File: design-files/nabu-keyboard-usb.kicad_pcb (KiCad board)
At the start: 2 copper layers, 55.2 x 71.8 mm, 20 parts, among them J1 Console UART header, J2 DIN-6, J3 9V input, Q1 IRLU110PBF, U1 74LVC245, U2 Pico, U3 SN75176AP

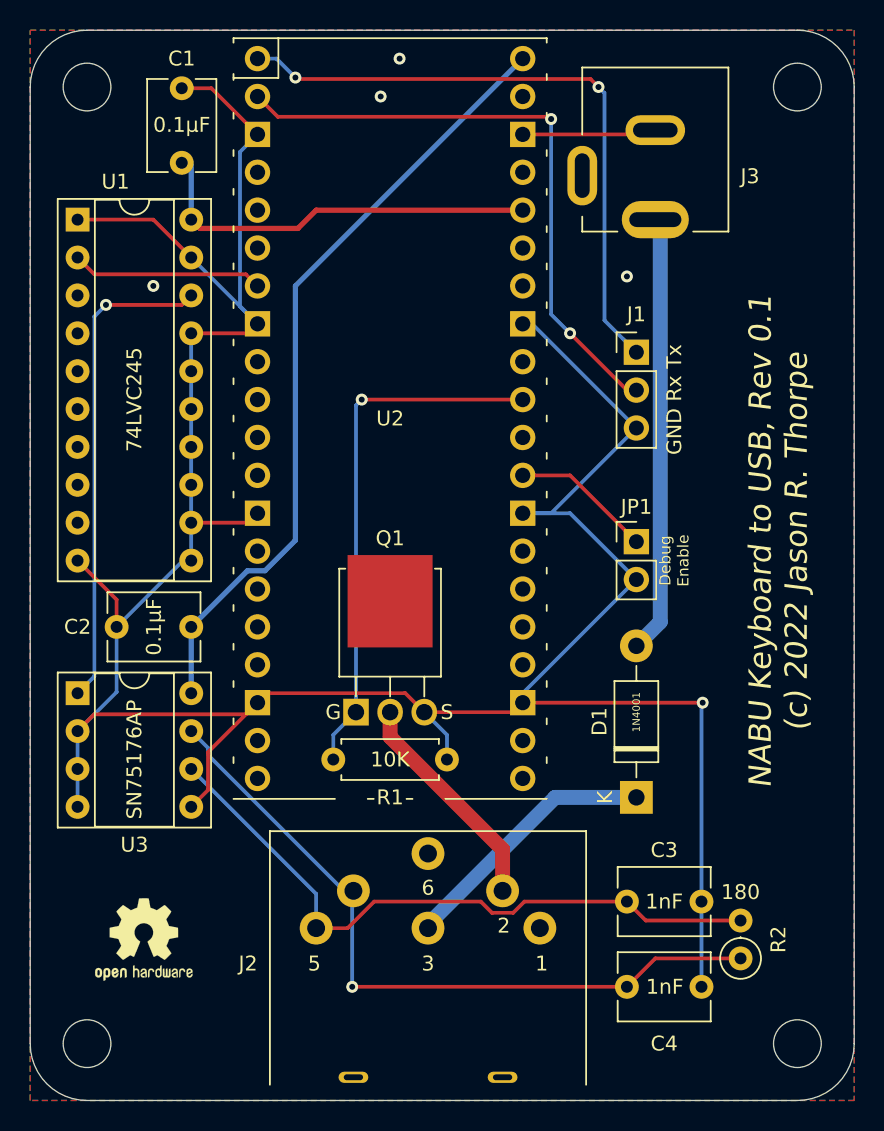
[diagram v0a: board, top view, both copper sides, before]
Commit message: Convert to KiCad 6 format.
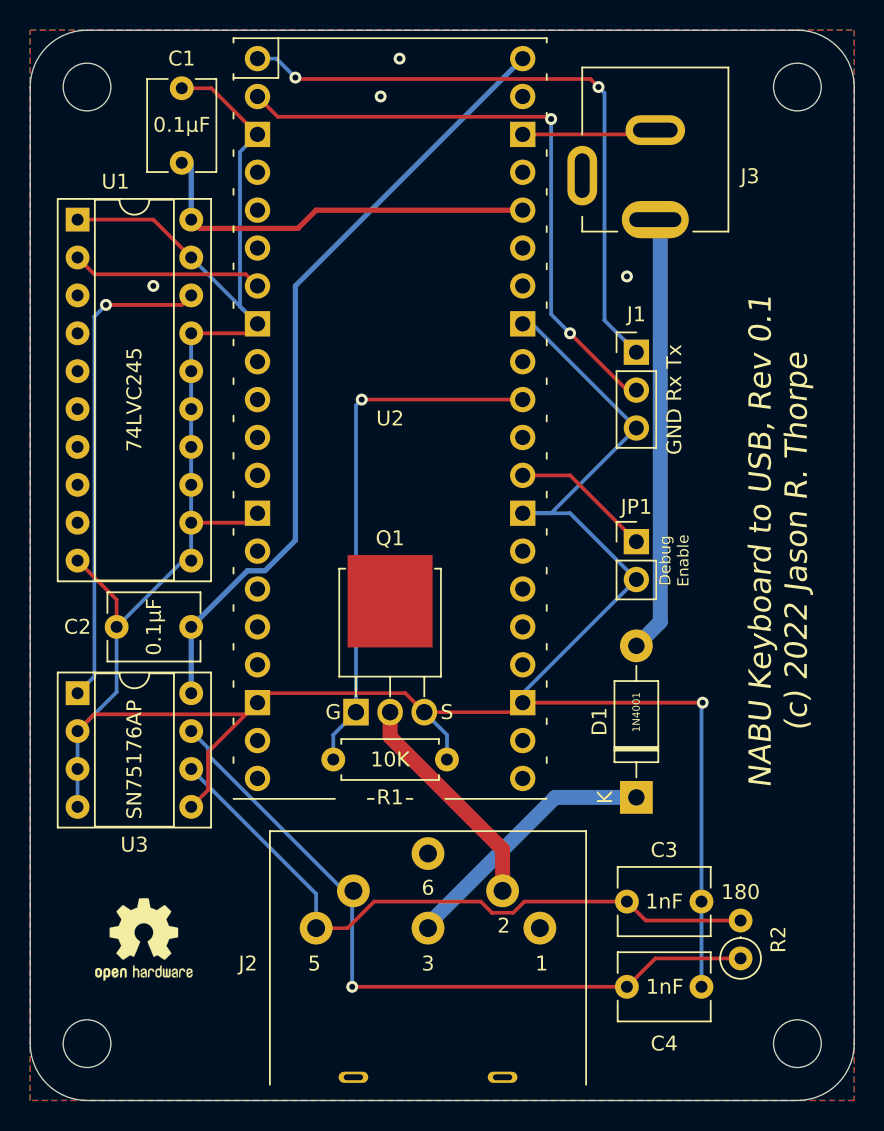
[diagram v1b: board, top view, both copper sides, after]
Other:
- net class Default removed
- net class HighPower removed
- net class LowPower removed

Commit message: Fix an error in the schematic that resulted in a non-working PCB; TX+ and TX- were swapped going into the 75176.
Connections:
- C3 pad 1: Net-(C3-Pad1) -> Net-(U3-Pad7)
- C4 pad 1: Net-(C4-Pad1) -> Net-(U3-Pad6)
- J2 pad 1: Net-(J2-Pad1) -> unconnected-(J2-Pad1)
- J2 pad 4: Net-(C4-Pad1) -> Net-(U3-Pad6)
- J2 pad 5: Net-(C3-Pad1) -> Net-(U3-Pad7)
- J2 pad 6: Net-(J2-Pad6) -> unconnected-(J2-Pad6)
- J3 pad 3: Net-(J3-Pad3) -> unconnected-(J3-Pad3)
- R2 pad 1: Net-(C4-Pad1) -> Net-(U3-Pad6)
- R2 pad 2: Net-(C3-Pad1) -> Net-(U3-Pad7)
- U1 pad 3: Net-(U1-Pad3) -> unconnected-(U1-Pad3)
- U1 pad 4: Net-(U1-Pad4) -> unconnected-(U1-Pad4)
- U1 pad 5: Net-(U1-Pad5) -> unconnected-(U1-Pad5)
- U1 pad 6: Net-(U1-Pad6) -> unconnected-(U1-Pad6)
- U1 pad 7: Net-(U1-Pad7) -> unconnected-(U1-Pad7)
- U1 pad 8: Net-(U1-Pad8) -> unconnected-(U1-Pad8)
- U1 pad 9: Net-(U1-Pad9) -> unconnected-(U1-Pad9)
- U2 pad 10: Net-(U2-Pad10) -> unconnected-(U2-Pad10)
- U2 pad 11: Net-(U2-Pad11) -> unconnected-(U2-Pad11)
- U2 pad 12: Net-(U2-Pad12) -> unconnected-(U2-Pad12)
- U2 pad 14: Net-(U2-Pad14) -> unconnected-(U2-Pad14)
- U2 pad 15: Net-(U2-Pad15) -> unconnected-(U2-Pad15)
- U2 pad 16: Net-(U2-Pad16) -> unconnected-(U2-Pad16)
- U2 pad 17: Net-(U2-Pad17) -> unconnected-(U2-Pad17)
- U2 pad 19: Net-(U2-Pad19) -> unconnected-(U2-Pad19)
- U2 pad 20: Net-(U2-Pad20) -> unconnected-(U2-Pad20)
- U2 pad 21: Net-(U2-Pad21) -> unconnected-(U2-Pad21)
- U2 pad 22: Net-(U2-Pad22) -> unconnected-(U2-Pad22)
- U2 pad 24: Net-(U2-Pad24) -> unconnected-(U2-Pad24)
- U2 pad 25: Net-(U2-Pad25) -> unconnected-(U2-Pad25)
- U2 pad 26: Net-(U2-Pad26) -> unconnected-(U2-Pad26)
- U2 pad 27: Net-(U2-Pad27) -> unconnected-(U2-Pad27)
- U2 pad 30: Net-(U2-Pad30) -> unconnected-(U2-Pad30)
- U2 pad 32: Net-(U2-Pad32) -> unconnected-(U2-Pad32)
- U2 pad 34: Net-(U2-Pad34) -> unconnected-(U2-Pad34)
- U2 pad 35: Net-(U2-Pad35) -> unconnected-(U2-Pad35)
- U2 pad 37: Net-(U2-Pad37) -> unconnected-(U2-Pad37)
- U2 pad 39: Net-(U2-Pad39) -> unconnected-(U2-Pad39)
- U2 pad 4: Net-(U2-Pad4) -> unconnected-(U2-Pad4)
- U2 pad 5: Net-(U2-Pad5) -> unconnected-(U2-Pad5)
- U2 pad 6: Net-(U2-Pad6) -> unconnected-(U2-Pad6)
- U2 pad 9: Net-(U2-Pad9) -> unconnected-(U2-Pad9)
- U3 pad 6: Net-(C3-Pad1) -> Net-(U3-Pad6)
- U3 pad 7: Net-(C4-Pad1) -> Net-(U3-Pad7)
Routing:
- net Net-(U3-Pad7): track 0.00 -> 49.0 mm
- net Net-(C4-Pad1): track 49.0 -> 0.00 mm, vias 1 -> 0
- net Net-(U3-Pad6): track 0.00 -> 47.7 mm, vias 0 -> 1
- net Net-(C3-Pad1): track 44.5 -> 0.00 mm

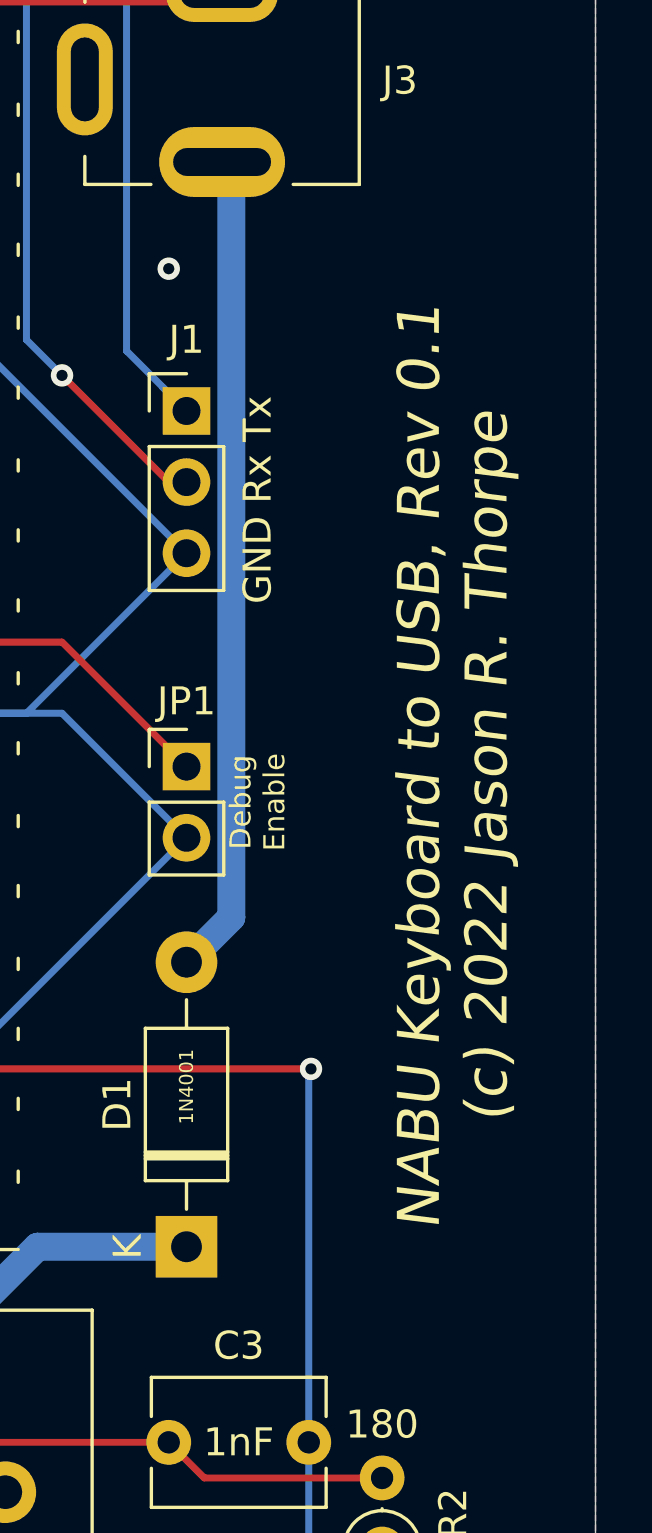
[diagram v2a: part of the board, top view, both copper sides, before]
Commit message: Update PCB silkscreen to reflect rev bump and make new font/back images.
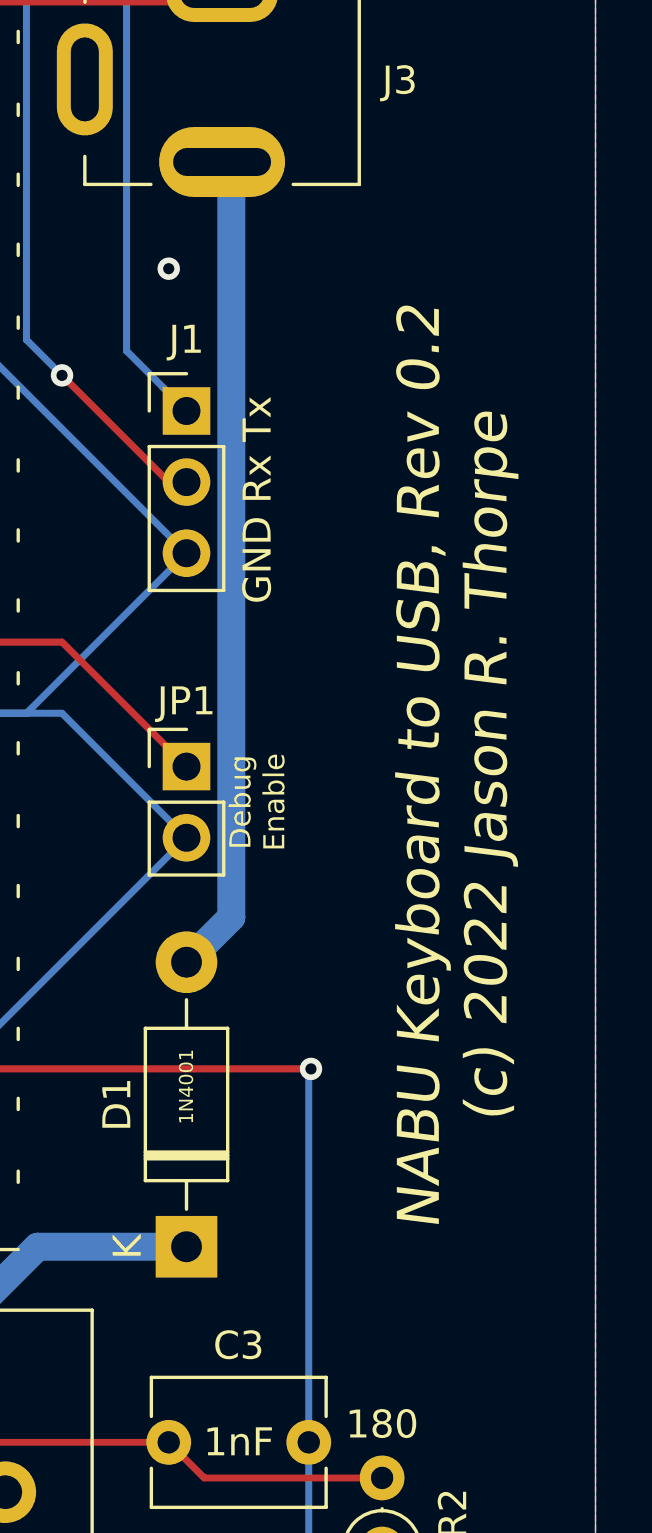
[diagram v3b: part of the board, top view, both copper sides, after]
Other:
- board text added: "NABU Keyboard to USB, Rev 0.2 (c) 2022 Jason R. Thorpe"
- board text removed: "NABU Keyboard to USB, Rev 0.1 (c) 2022 Jason R. Thorpe"
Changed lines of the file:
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@@
     (effects (font (size 1 1) (thickness 0.15)))
   )
-  (gr_text "NABU Keyboard to USB, Rev 0.1\n(c) 2022 Jason R. Thorpe" (at 167.64 97.79 90) (layer "F.SilkS")
+  (gr_text "NABU Keyboard to USB, Rev 0.2\n(c) 2022 Jason R. Thorpe" (at 167.64 97.79 90) (layer "F.SilkS")
     (effects (font (size 1.5 1.5) (thickness 0.3) italic))
   )
